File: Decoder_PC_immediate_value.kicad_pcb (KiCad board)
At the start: 4 copper layers, 81.4 x 51.2 mm, 29 parts, among them Q1 BC818

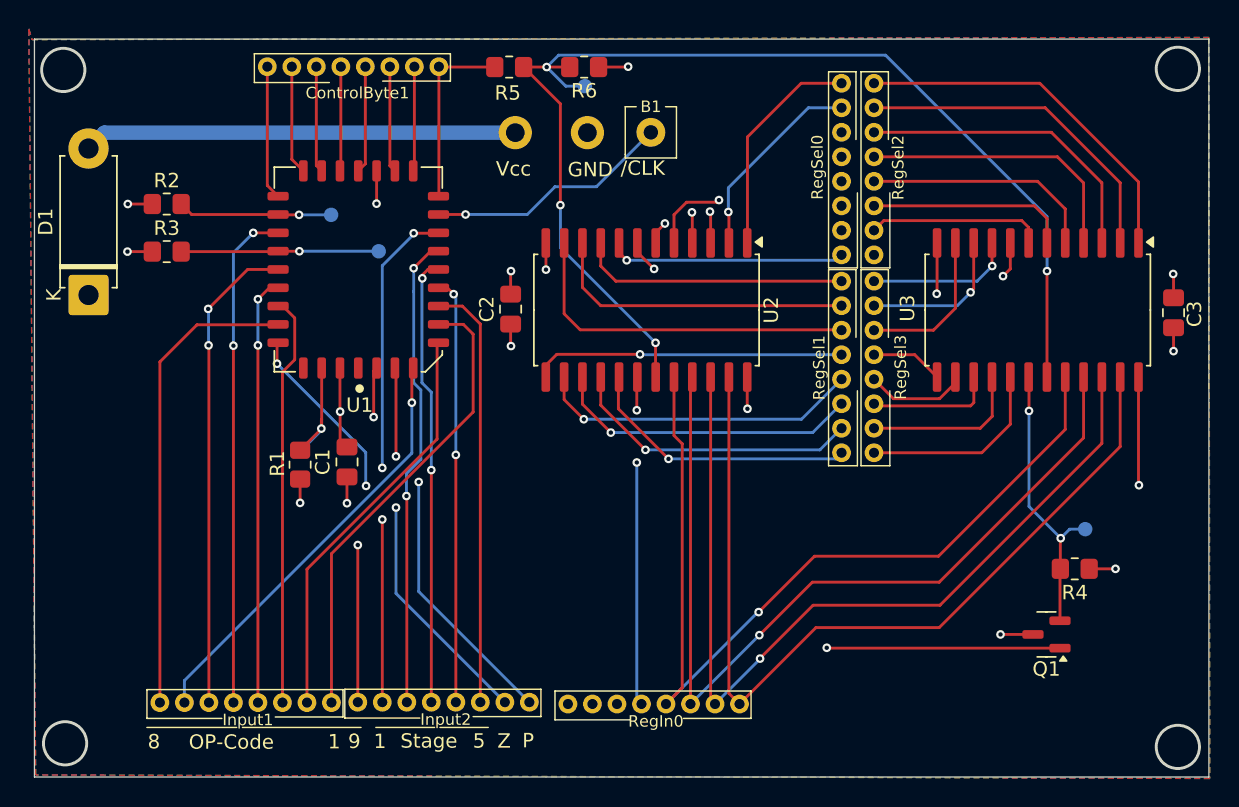
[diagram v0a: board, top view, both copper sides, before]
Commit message: Added Bulk Capacitor
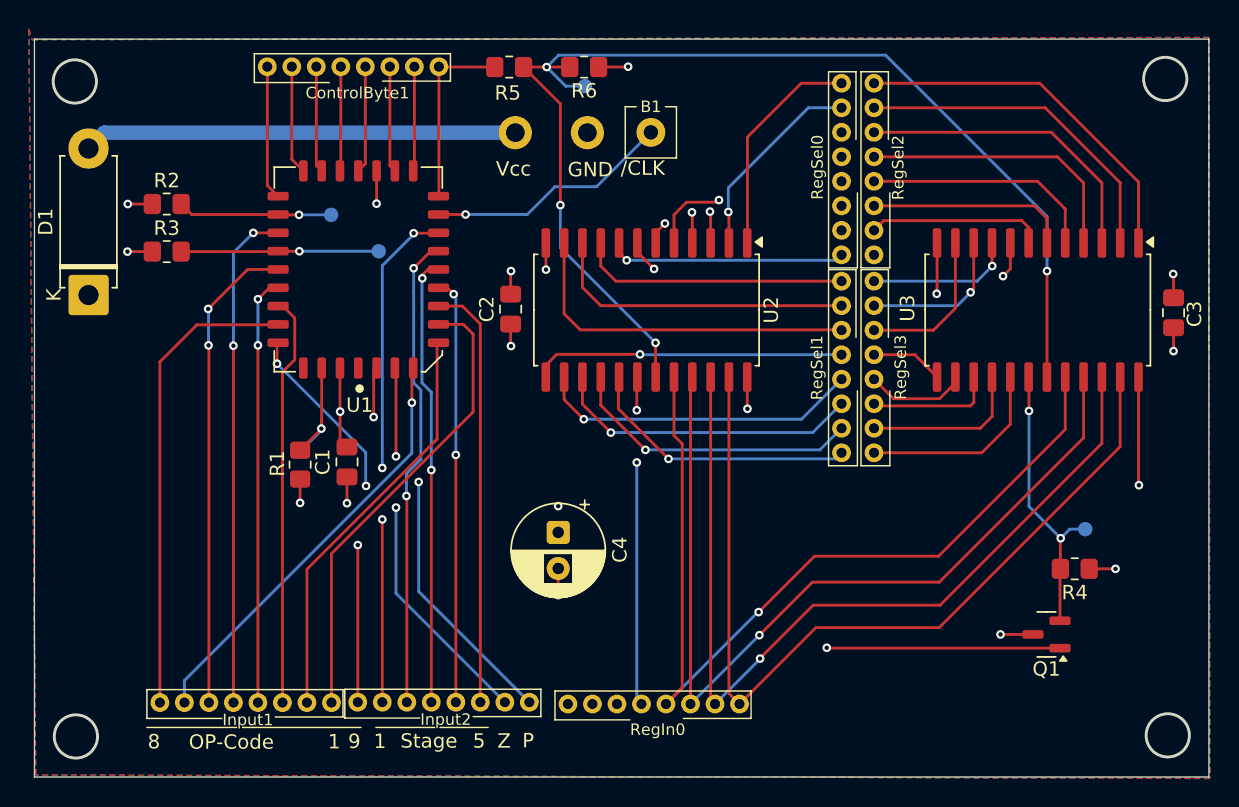
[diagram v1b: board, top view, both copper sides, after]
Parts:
- added C4: C_Polarized, Capacitor_THT:CP_Radial_D6.3mm_P2.50mm, F.Cu at (108.6, 93.4)
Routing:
- net GND: track 18.4 -> 20.3 mm, vias 9 -> 10
- net VCC: vias 8 -> 9
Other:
- outline, holes or cut-outs redrawn

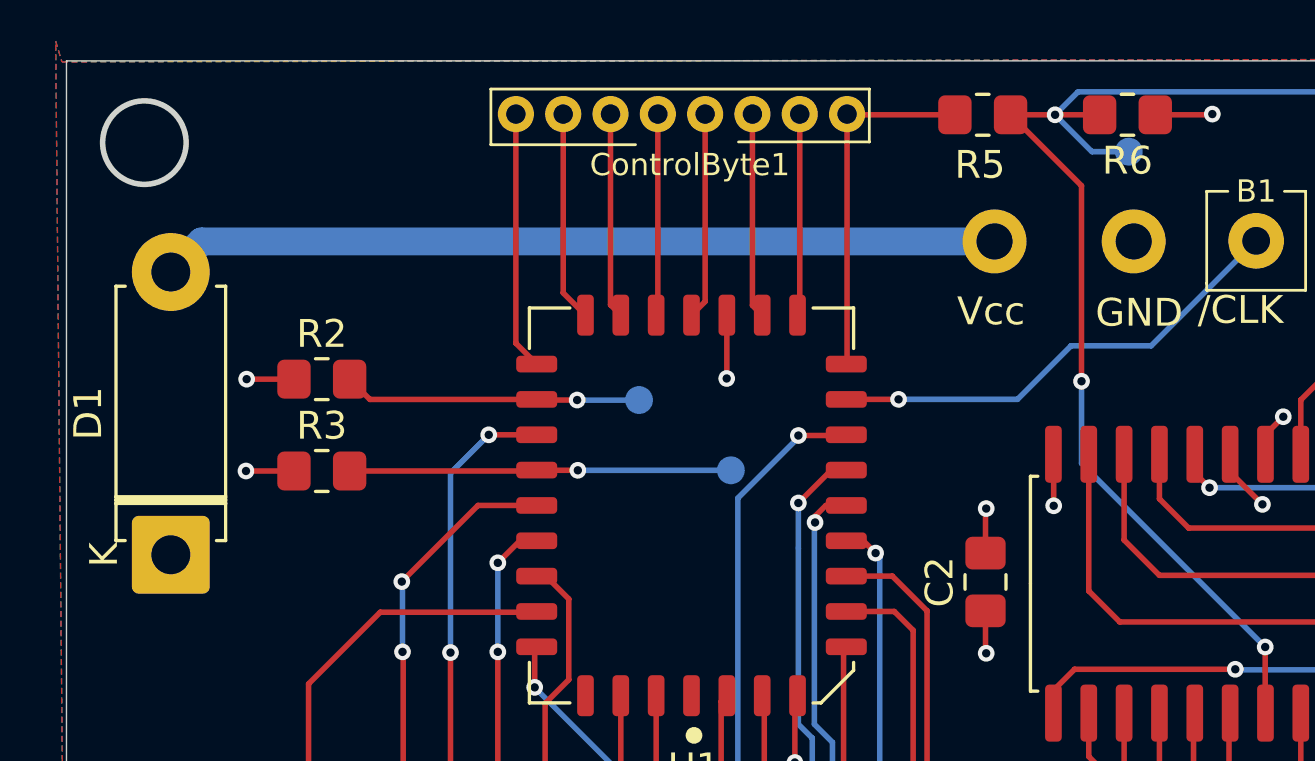
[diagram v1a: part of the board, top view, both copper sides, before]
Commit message: Corrected Position of Diode
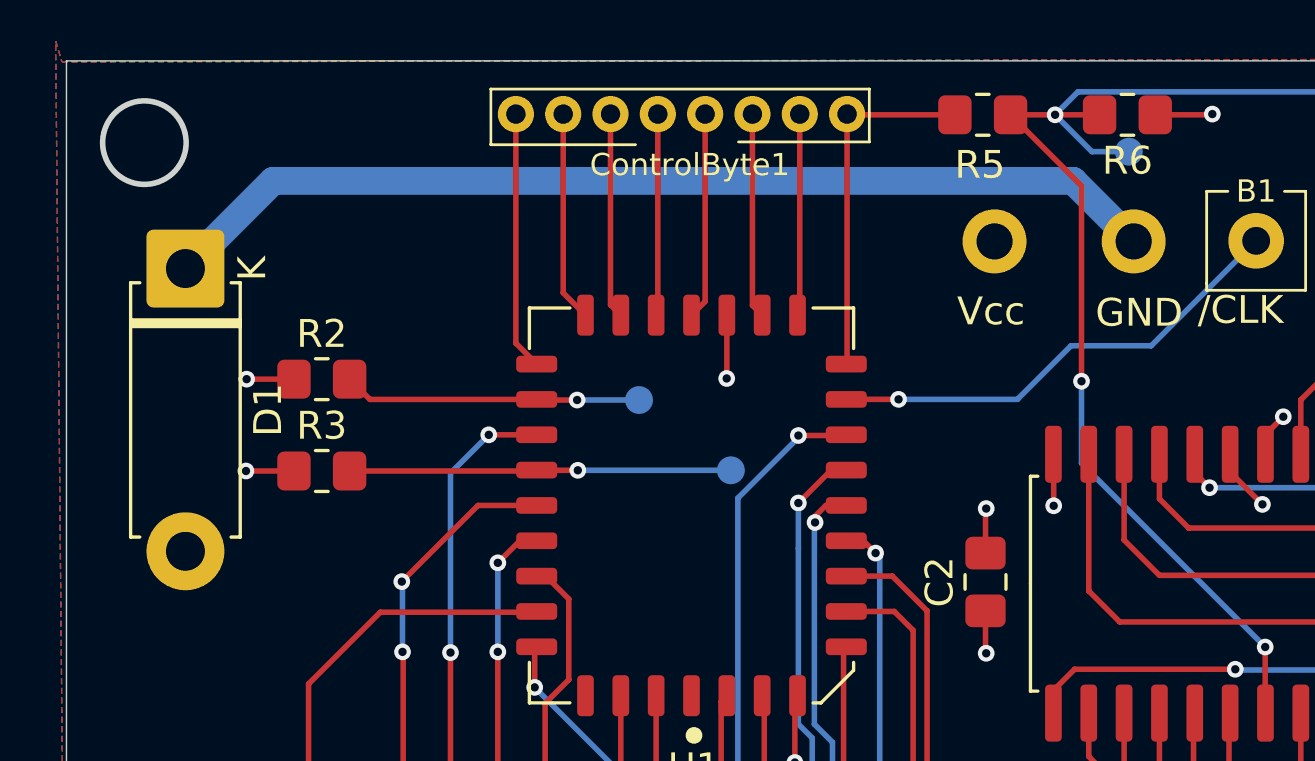
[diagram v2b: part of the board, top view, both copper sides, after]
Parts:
- moved D1 10.3 mm to (76.5, 66.7), turned to -90 degrees
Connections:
- D1 pad 1: VCC -> Net-(D1-K)
- D1 pad 2: Net-(D1-A) -> GND
- U5 pad 1: Net-(D1-A) -> VCC
- U5 pad 2: GND -> Net-(D1-K)
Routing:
- net Net-(D1-K): track 0.00 -> 36.3 mm
- net Net-(D1-A): track 30.1 -> 0.00 mm
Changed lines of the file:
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@@
 	(net 72 "Net-(U3-Y9)")
 	(net 73 "Net-(U3-Y12)")
-	(net 74 "Net-(D1-A)")
+	(net 74 "Net-(D1-K)")
 	(net 75 "{slash}REG_ACT")
 	(footprint "Capacitor_SMD:C_0805_2012Metric_Pad1.18x1.45mm_HandSolder"
@@
 			(layers "*.Cu" "*.Mask")
 			(remove_unused_layers no)
-			(net 74 "Net-(D1-A)")
+			(net 25 "VCC")
 			(pinfunction "Vcc")
 			(pintype "power_out")
@@
 			(layers "*.Cu" "*.Mask")
 			(remove_unused_layers no)
-			(net 9 "GND")
+			(net 74 "Net-(D1-K)")
 			(pinfunction "GND")
 			(pintype "power_out")
@@
 	(footprint "Diode_THT:D_5W_P10.16mm_Horizontal"
 		(layer "F.Cu")
-		(at 76 76.935 90)
+		(at 76.525 66.65 -90)
 		(descr "Diode, 5W series, Axial, Horizontal, pin pitch=10.16mm, length*diameter=8.9*3.7mm^2, http://www.diodes.com/_files/packages/8686949.gif")
 		(tags "Diode 5W series Axial Horizontal pin pitch 10.16mm  length 8.9mm diameter 3.7mm")
@@
 		)
 		(property "Sim.Device" "D"
-			(at 0 0 90)
+			(at 0 0 270)
 			(unlocked yes)
 			(layer "F.Fab")
@@
 		)
 		(property "Sim.Pins" "1=K 2=A"
-			(at 0 0 90)
+			(at 0 0 270)
 			(unlocked yes)
 			(layer "F.Fab")
@@
 		(attr through_hole)
 		(fp_line
-			(start 9.65 -1.97)
-			(end 9.65 -1.64)
+			(start 0.51 1.97)
+			(end 9.65 1.97)
 			(stroke
 				(width 0.12)
@@
 		)
 		(fp_line
-			(start 2.085 -1.97)
-			(end 2.085 1.97)
+			(start 9.65 1.97)
+			(end 9.65 1.64)
 			(stroke
 				(width 0.12)
@@
 		)
 		(fp_line
-			(start 1.965 -1.97)
-			(end 1.965 1.97)
+			(start 0.51 1.64)
+			(end 0.51 1.97)
 			(stroke
 				(width 0.12)
@@
 		)
 		(fp_line
-			(start 1.845 -1.97)
-			(end 1.845 1.97)
+			(start 0.51 -1.64)
+			(end 0.51 -1.97)
 			(stroke
 				(width 0.12)
@@
 		)
 		(fp_line
-			(start 0.51 -1.64)
-			(end 0.51 -1.97)
+			(start 1.845 -1.97)
+			(end 1.845 1.97)
 			(stroke
 				(width 0.12)
@@
 		)
 		(fp_line
-			(start 0.51 1.64)
-			(end 0.51 1.97)
+			(start 1.965 -1.97)
+			(end 1.965 1.97)
 			(stroke
 				(width 0.12)
@@
 		)
 		(fp_line
-			(start 9.65 1.97)
-			(end 9.65 1.64)
+			(start 2.085 -1.97)
+			(end 2.085 1.97)
 			(stroke
 				(width 0.12)
@@
 		)
 		(fp_line
-			(start 0.51 1.97)
-			(end 9.65 1.97)
+			(start 9.65 -1.97)
+			(end 9.65 -1.64)
 			(stroke
 				(width 0.12)
@@
 		)
 		(fp_line
-			(start 2.065 -1.85)
-			(end 2.065 1.85)
+			(start 0 0)
+			(end 0.63 0)
 			(stroke
 				(width 0.1)
@@
 		)
 		(fp_line
-			(start 1.965 -1.85)
-			(end 1.965 1.85)
+			(start 10.16 0)
+			(end 9.53 0)
 			(stroke
 				(width 0.1)
@@
 		)
 		(fp_line
-			(start 10.16 0)
-			(end 9.53 0)
+			(start 1.965 -1.85)
+			(end 1.965 1.85)
 			(stroke
 				(width 0.1)
@@
 		)
 		(fp_line
-			(start 0 0)
-			(end 0.63 0)
+			(start 2.065 -1.85)
+			(end 2.065 1.85)
 			(stroke
 				(width 0.1)
@@
 		)
 		(pad "1" thru_hole roundrect
-			(at 0 0 90)
+			(at 0 0 270)
 			(size 2.8 2.8)
 			(drill 1.4)
@@
 			(remove_unused_layers no)
 			(roundrect_rratio 0.089286)
-			(net 25 "VCC")
+			(net 74 "Net-(D1-K)")
 			(pinfunction "K")
 			(pintype "passive")
 		)
 		(pad "2" thru_hole circle
-			(at 10.16 0 90)
+			(at 10.16 0 270)
 			(size 2.8 2.8)
 			(drill 1.4)
 			(layers "*.Cu" "*.Mask")
 			(remove_unused_layers no)
-			(net 74 "Net-(D1-A)")
+			(net 9 "GND")
 			(pinfunction "A")
 			(pintype "passive")
@@
 	)
 	(segment
-		(start 77.1 65.675)
-		(end 76 66.775)
+		(start 79.675 63.5)
+		(end 76.525 66.65)
+		(width 1)
+		(layer "B.Cu")
+		(net 74)
+	)
+	(segment
+		(start 108.425 63.5)
+		(end 79.675 63.5)
 		(width 1)
 		(layer "B.Cu")
@@
 	)
 	(segment
-		(start 105.6 65.675)
-		(end 77.1 65.675)
+		(start 110.6 65.675)
+		(end 108.425 63.5)
 		(width 1)
 		(layer "B.Cu")
